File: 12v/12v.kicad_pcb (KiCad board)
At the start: 2 copper layers, 43.2 x 61 mm, 46 parts, among them J1 Conn_01x08_Female, J2 Conn_01x01, J3 12v+, J4 GNDPWR, J5 Conn_01x01, Q1 FET_A_UP, Q2 FET_A_DOWN, Q3 FET_B_UP, Q4 FET_B_DOWN, U1 7400, U2 IRS2108, U3 TLP2955, U4 TLP2955, U5 IRS2108

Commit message: draw gerber data
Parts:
- added J6: Conn_02x08_Counter_Clockwise, Pin_Headers:Pin_Header_Straight_2x08_Pitch2.54mm, F.Cu at (94.7, 68.6)
- added J7: Conn_02x08_Counter_Clockwise, Pin_Headers:Pin_Header_Straight_2x08_Pitch2.54mm, F.Cu at (161.3, 88.9)
- J3: value 12v+ -> Conn_02x08_Counter_Clockwise; footprint Pin_Headers:Pin_Header_Straight_2x10_Pitch2.54mm -> Pin_Headers:Pin_Header_Straight_2x08_Pitch2.54mm
- J4: value GNDPWR -> Conn_02x08_Counter_Clockwise; footprint Pin_Headers:Pin_Header_Straight_2x10_Pitch2.54mm -> Pin_Headers:Pin_Header_Straight_2x08_Pitch2.54mm
- moved J4 112.5 mm to (94.7, 88.9)
- moved C6 87.4 mm to (106.7, 71.1), turned to 180 degrees
- moved R5 81.1 mm to (112.3, 83.1), turned to 0 degrees
- moved J2 80.9 mm to (102.9, 105.4)
- moved D8 77.0 mm to (116.8, 69.8), turned to 270 degrees
- moved Q1 76.8 mm to (109.2, 81.3), turned to 90 degrees
- moved J5 74.5 mm to (108.0, 105.4)
- moved R12 73.2 mm to (118.1, 67.3), turned to 180 degrees
- moved Q2 73.2 mm to (109.2, 88.4), turned to 90 degrees
- moved D3 72.8 mm to (120.1, 87.6), turned to 180 degrees
- moved Q4 71.0 mm to (109.2, 95.2), turned to 90 degrees
- moved R3 70.6 mm to (114.6, 79.8), turned to 0 degrees
- moved Q3 70.2 mm to (109.2, 102.4), turned to 90 degrees
- moved R11 68.3 mm to (111.3, 95.5), turned to 0 degrees
- moved R4 67.8 mm to (112.5, 85.1), turned to 0 degrees
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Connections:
- J4 pad 1: GNDPWR -> +12V
- J4 pad 10: GNDPWR -> +12V
- J4 pad 11: GNDPWR -> +12V
- J4 pad 12: GNDPWR -> +12V
- J4 pad 13: GNDPWR -> +12V
- J4 pad 14: GNDPWR -> +12V
- J4 pad 15: GNDPWR -> +12V
- J4 pad 16: GNDPWR -> +12V
- J4 pad 2: GNDPWR -> +12V
- J4 pad 3: GNDPWR -> +12V
- J4 pad 4: GNDPWR -> +12V
- J4 pad 5: GNDPWR -> +12V
- J4 pad 6: GNDPWR -> +12V
- J4 pad 7: GNDPWR -> +12V
- J4 pad 8: GNDPWR -> +12V
- J4 pad 9: GNDPWR -> +12V
- U3 pad 1: Net-(U3-Pad1) -> (no net)
- U3 pad 4: Net-(U3-Pad4) -> (no net)
- U3 pad 6: Net-(U3-Pad6) -> (no net)
- U4 pad 1: Net-(U4-Pad1) -> (no net)
- U4 pad 4: Net-(U4-Pad4) -> (no net)
- U4 pad 6: Net-(U4-Pad6) -> (no net)
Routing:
- net +12V: track 34.0 -> 119.7 mm, vias 0 -> 1
- net GNDPWR: track 57.6 -> 139.5 mm, vias 0 -> 2
- net GND: track 0.00 -> 65.7 mm
- net +5V: track 0.00 -> 50.5 mm
- net INB: track 0.00 -> 46.1 mm
- net OUTB: track 0.00 -> 42.9 mm, vias 0 -> 3
- net INA: track 0.00 -> 42.7 mm, vias 0 -> 2
- net PWM: track 0.00 -> 40.7 mm
- net OUTA: track 0.00 -> 24.5 mm, vias 0 -> 2
- net Net-(U1-Pad8): track 0.00 -> 22.0 mm
- net Net-(C7-Pad2): track 33.7 -> 53.1 mm
- net Net-(R2-Pad2): track 0.00 -> 15.1 mm, vias 0 -> 1
- net Net-(C3-Pad2): track 43.8 -> 58.4 mm, vias 0 -> 1
- net Net-(D10-Pad1): track 0.00 -> 14.1 mm
- net Net-(R1-Pad2): track 0.00 -> 13.4 mm
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- added copper zone on B.Cu, net +12V
- added copper zone on F.Cu, net +12V
- added copper zone on B.Cu, net GND
- added copper zone on F.Cu, net GND
- added copper zone on B.Cu, net GNDPWR
- added copper zone on F.Cu, net GNDPWR
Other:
- board size 43.2 x 61 mm -> 71.9 x 41.7 mm

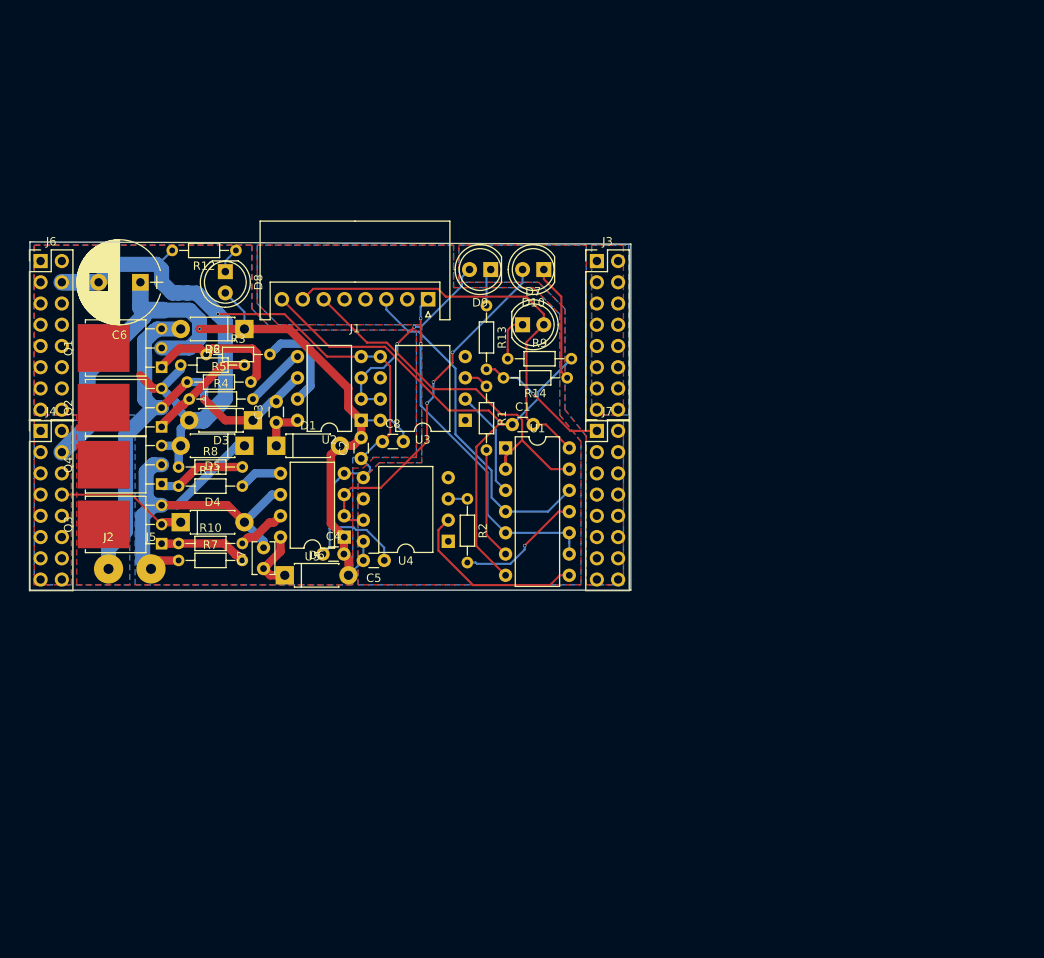
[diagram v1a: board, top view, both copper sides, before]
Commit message: use SMD parts.(Not Wired)
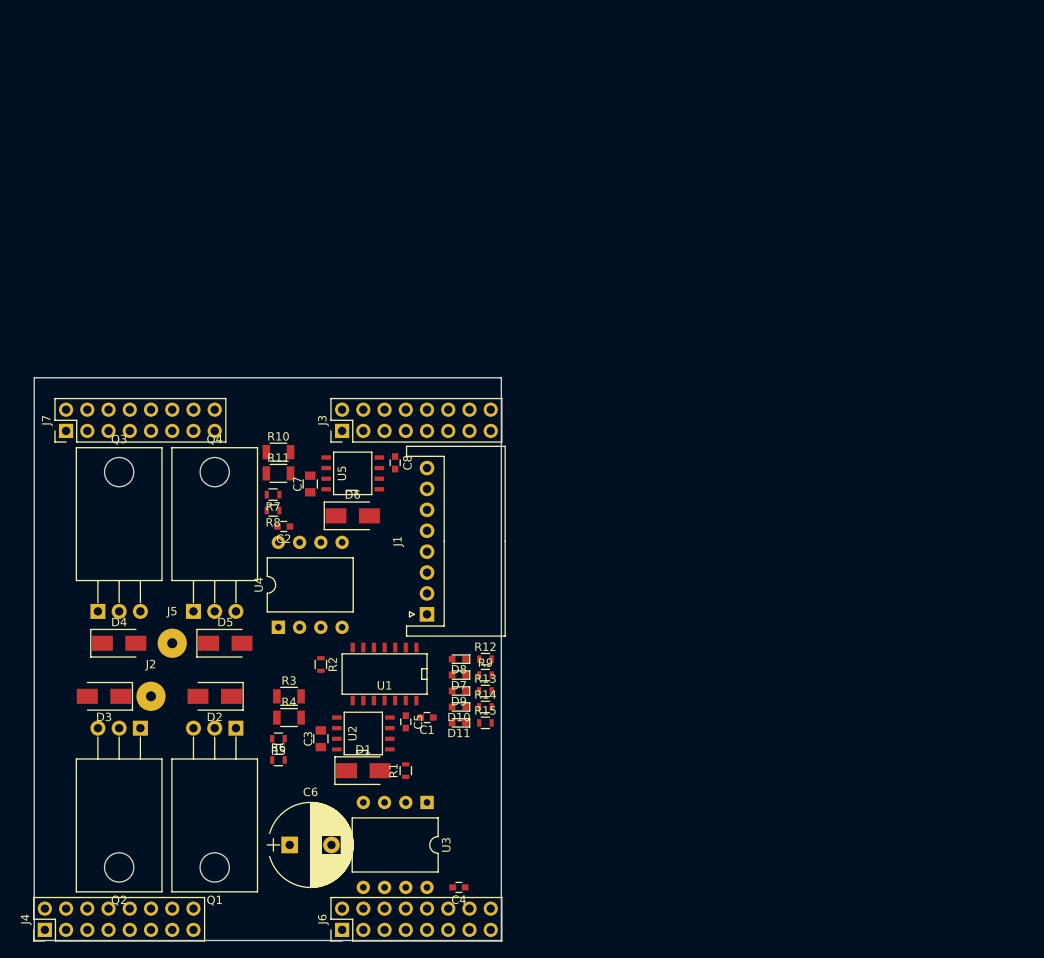
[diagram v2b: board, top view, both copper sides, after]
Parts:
- added D11: LED, LEDs:LED_0603, F.Cu at (144.8, 123.8)
- added R15: R, Resistors_SMD:R_0603, F.Cu at (148.0, 123.8)
- C1, C2, C4, C5, C8: footprint Capacitors_THT:C_Disc_D3.0mm_W1.6mm_P2.50mm -> Capacitors_SMD:C_0603
- C3: footprint Capacitors_THT:C_Disc_D3.0mm_W1.6mm_P2.50mm -> Capacitors_SMD:C_0805
- C7: footprint Capacitors_THT:C_Disc_D3.8mm_W2.6mm_P2.50mm -> Capacitors_SMD:C_0805
- D1, D2, D3, D4, D5, D6: footprint Diodes_THT:D_DO-41_SOD81_P7.62mm_Horizontal -> Diodes_SMD:D_SMA
- D10, D7, D8, D9: footprint LEDs:LED_D5.0mm -> LEDs:LED_0603
- Q1, Q2, Q3, Q4: footprint TO_SOT_Packages_THT:TO-251-1EP_IPAK_Horizontal -> TO_SOT_Packages_THT:TO-220-3_Horizontal
- R1, R12, R13, R14, R2, R5, R6, R7, R8: footprint Resistors_THT:R_Axial_DIN0204_L3.6mm_D1.6mm_P7.62mm_Horizontal -> Resistors_SMD:R_0603
- R10, R11, R3, R4: footprint Resistors_THT:R_Axial_DIN0204_L3.6mm_D1.6mm_P7.62mm_Horizontal -> Resistors_SMD:R_1206
- R9: value R -> LEDR; footprint Resistors_THT:R_Axial_DIN0204_L3.6mm_D1.6mm_P7.62mm_Horizontal -> Resistors_SMD:R_0603
- U1: footprint Housings_DIP:DIP-14_W7.62mm -> SMD_Packages:SOIC-14_N
- U2, U5: value IRS2108 -> IRS2302; footprint Housings_DIP:DIP-8_W7.62mm -> SMD_Packages:SOIC-8-N
- moved J6 87.8 mm to (130.8, 148.6), turned to 90 degrees
- moved C6 69.6 mm to (124.5, 138.4), turned to 0 degrees
- moved J7 63.5 mm to (97.8, 88.9), turned to 90 degrees
- moved J4 59.7 mm to (95.2, 148.6), turned to 90 degrees
- moved R12 57.3 mm to (148.0, 116.2), turned to 0 degrees
- moved D8 54.1 mm to (144.8, 116.2), turned to 180 degrees
- moved D10 53.3 mm to (144.8, 121.9)
- moved D9 50.6 mm to (144.8, 120.0)
- moved R6 48.7 mm to (123.2, 128.3)
- moved R1 47.0 mm to (138.4, 129.5), turned to 90 degrees
- moved R13 46.1 mm to (148.0, 120.0), turned to 0 degrees
- moved U3 45.9 mm to (141.0, 133.3), turned to 270 degrees
- moved D2 44.1 mm to (115.6, 120.7)
- moved Q1 44.1 mm to (118.1, 124.5), turned to 180 degrees
- moved R5 44.0 mm to (123.2, 125.7), turned to 180 degrees
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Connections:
- D10 pad 2: OUTB -> INB
- D9 pad 2: OUTA -> INA
- R13 pad 2: GNDPWR -> GND
- R14 pad 2: GNDPWR -> GND
- U2 pad 3: OUTA -> +12V
- U5 pad 3: OUTB -> +12V
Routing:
- net GNDPWR: track 139.5 -> 0.00 mm, vias 2 -> 0
- net +12V: track 119.7 -> 0.00 mm, vias 1 -> 0
- net GND: track 65.7 -> 0.00 mm
- net Net-(C3-Pad2): track 58.4 -> 0.00 mm, vias 1 -> 0
- net Net-(C7-Pad2): track 53.1 -> 0.00 mm
- net +5V: track 50.5 -> 0.00 mm
- net INB: track 46.1 -> 0.00 mm
- net OUTB: track 42.9 -> 0.00 mm, vias 3 -> 0
- net INA: track 42.7 -> 0.00 mm, vias 2 -> 0
- net PWM: track 40.7 -> 0.00 mm
- net OUTA: track 24.5 -> 0.00 mm, vias 2 -> 0
- net Net-(U1-Pad8): track 22.0 -> 0.00 mm
- net Net-(Q1-Pad1): track 16.9 -> 0.00 mm
- net Net-(R2-Pad2): track 15.1 -> 0.00 mm, vias 1 -> 0
- net Net-(D10-Pad1): track 14.1 -> 0.00 mm
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- removed copper zone on B.Cu, net +12V
- removed copper zone on F.Cu, net +12V
- removed copper zone on B.Cu, net GND
- removed copper zone on F.Cu, net GND
- removed copper zone on B.Cu, net GNDPWR
- removed copper zone on F.Cu, net GNDPWR
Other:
- board size 71.9 x 41.7 mm -> 55.9 x 67.3 mm
- rule trace_min: 0.2 -> 0.25

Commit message: wiring
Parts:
- moved C1 3.42 mm to (142.2, 120.0), turned to 270 degrees
- moved R2 1.79 mm to (128.3, 115.0)
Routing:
- net +12V: track 0.00 -> 243.7 mm, vias 0 -> 2
- net GNDPWR: track 0.00 -> 194.1 mm, vias 0 -> 4
- net GND: track 0.00 -> 58.8 mm
- net Net-(C3-Pad2): track 0.00 -> 46.2 mm
- net Net-(C7-Pad2): track 0.00 -> 45.0 mm
- net Net-(Q3-Pad1): track 0.00 -> 33.9 mm
- net INB: track 0.00 -> 32.8 mm, vias 0 -> 3
- net PWM: track 0.00 -> 30.3 mm, vias 0 -> 3
- net +5V: track 0.00 -> 29.7 mm
- net INA: track 0.00 -> 28.0 mm, vias 0 -> 3
- net Net-(Q2-Pad1): track 0.00 -> 24.4 mm
- net Net-(Q4-Pad1): track 0.00 -> 24.1 mm
- net Net-(U1-Pad3): track 0.00 -> 20.8 mm, vias 0 -> 1
- net OUTA: track 0.00 -> 19.9 mm, vias 0 -> 1
- net Net-(R1-Pad2): track 0.00 -> 17.5 mm, vias 0 -> 2
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- added copper zone on B.Cu, net +12V
- added copper zone on B.Cu, net GND
- added copper zone on F.Cu, net GND
- added copper zone on B.Cu, net GNDPWR
- added copper zone on F.Cu, net GNDPWR
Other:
- net class Default: via_dia 0.4 -> 0.6
- net class Power: via_dia 0.4 -> 0.6
- rule trace_min: 0.25 -> 0
- rule via_min_size: 0.4 -> 0.6
